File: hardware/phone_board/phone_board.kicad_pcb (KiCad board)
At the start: 4 copper layers, 66 x 36 mm, 70 parts, among them J1 TYPE-C-31-M-12, J2 LiPo 1S, Q1 AO3401A, SW1 POWER, SW2 RESET, SW3 BOOT, U1 USBLC6-2SC6, U2 BQ24073RGTR, U3 AP2112K-3.3, U4 TPS61023DRLR, U5 ESP32-S3-MINI-1-N8, U6 ADS1115IDGSR, U7 SHT40-AD1B

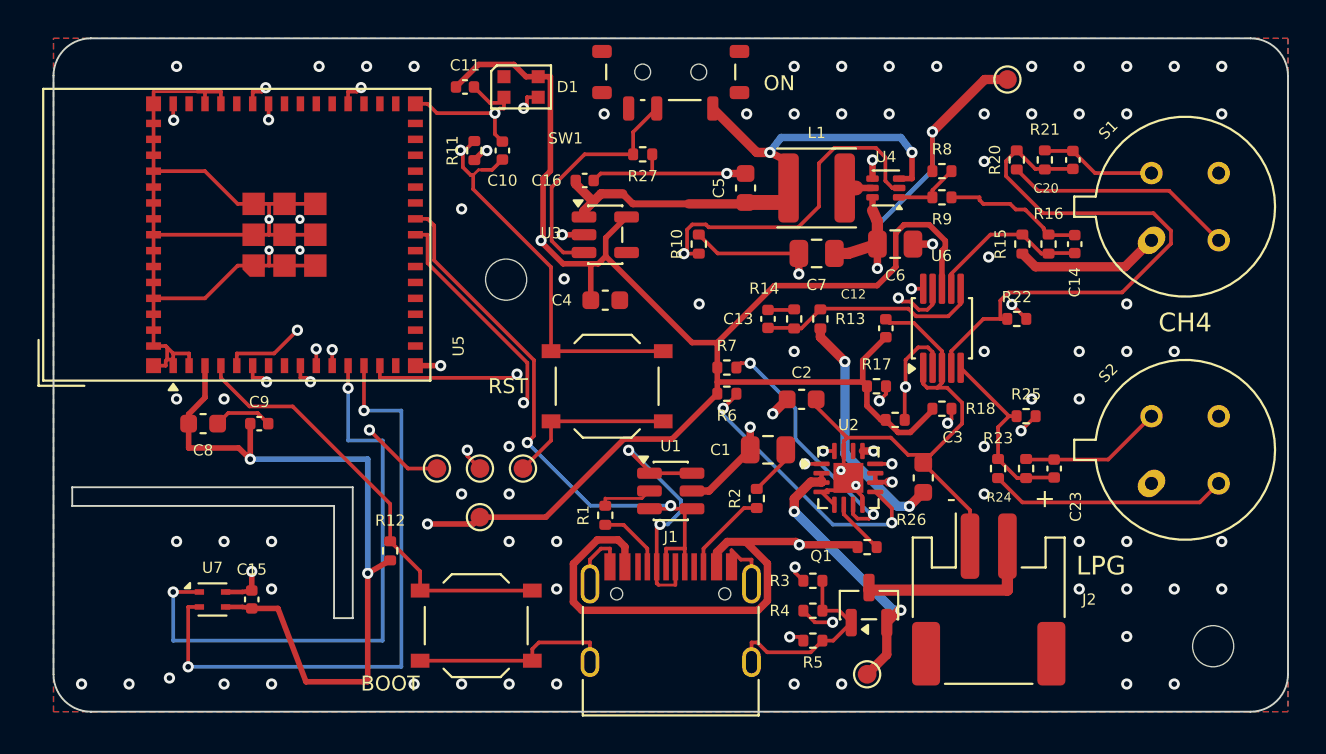
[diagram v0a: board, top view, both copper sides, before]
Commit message: Phone board rev C: compact the layout to 60 x 33 mm
Same schematic, parts and block arrangement as the fabricated rev B, with the
empty board area removed. The hand-routed blocks move as rigid units (MCU
column and SHT40 tongue 2 mm up, power/USB column with the boost loop 2 mm
left); only the free-form right third is re-packed: cans flush at the right
edge, JST-PH under them exiting through the right edge, ADC and sensor
networks in one column, RESET above BOOT, serial test pads as a labelled
2 x 2 grid. Adds a GND via stub for the USB ESD diode, whose pour island had
none. Re-routed with Freerouting: 0 DRC, 0 unconnected, 0 parity, ERC clean.
Regenerated fab files, JLC placement and renders.

Enclosure: parameters updated for rev C and the battery opening moved to the
right wall; STLs not regenerated (no OpenSCAD here) and the H1 hold-down boss
now sits under a 60 x 35 mm cell, noted in its README.
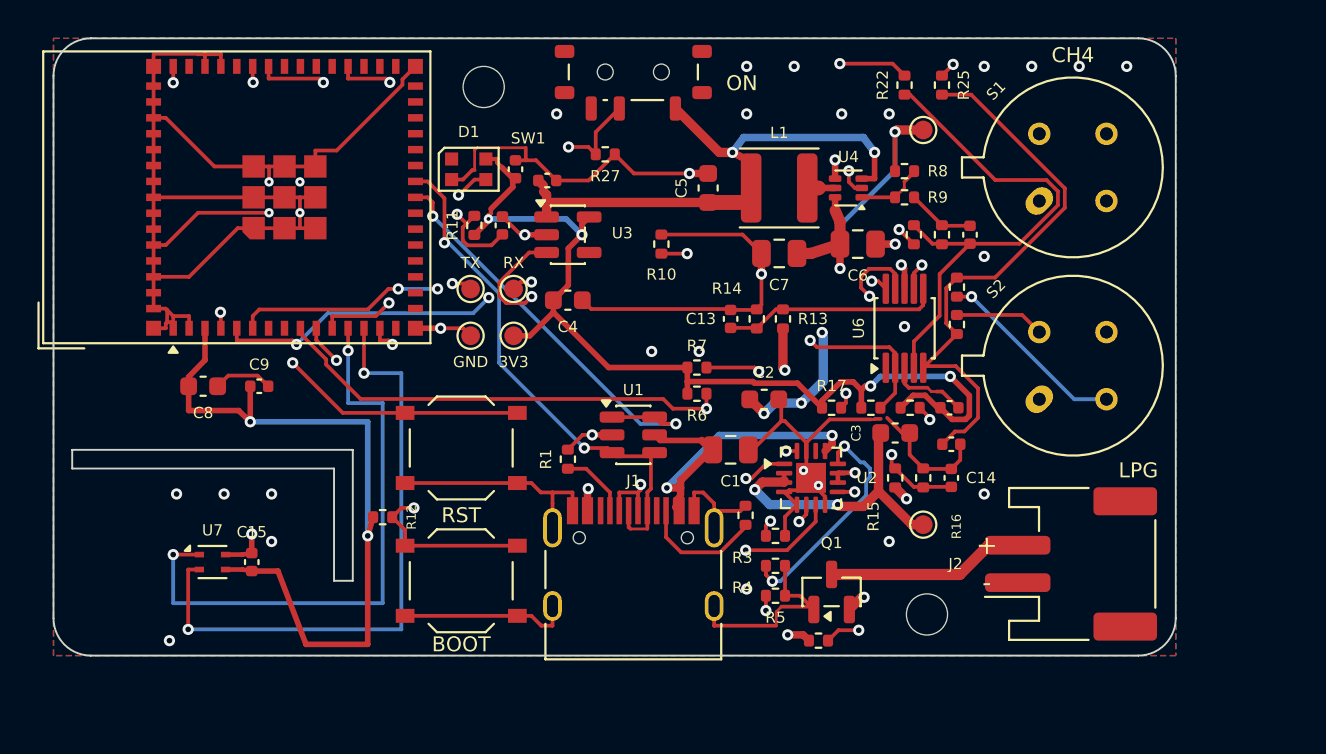
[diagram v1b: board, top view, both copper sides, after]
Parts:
- moved R25 18.3 mm to (47.5, 2.50), turned to 90 degrees
- moved H1 15.4 mm to (46.7, 30.8)
- moved R15 14.2 mm to (45.0, 23.5)
- moved R16 14.2 mm to (46.5, 23.5)
- moved C14 14.1 mm to (48.0, 23.5)
- moved R22 13.9 mm to (45.5, 2.50), turned to 90 degrees
- moved H2 10.4 mm to (23.0, 2.60)
- moved R23 9.95 mm to (48.3, 13.3)
- moved TP4 9.87 mm to (24.6, 15.9)
- moved TP1 9.77 mm to (22.3, 13.4)
- moved TP2 9.77 mm to (24.6, 13.4)
- moved TP5 8.54 mm to (46.5, 26.0)
- moved R24 8.54 mm to (48.3, 15.3)
- moved SW2 8.47 mm to (21.8, 21.9)
- moved TP3 7.63 mm to (22.3, 15.9)
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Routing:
- net /LPG_TAP: track 10.0 -> 30.6 mm
- net /+3V3: track 139.3 -> 119.1 mm, vias 5 -> 7
- net /VBUS: track 51.2 -> 37.5 mm, vias 3 -> 4
- net /LPG_FB: track 55.9 -> 45.6 mm, vias 2 -> 3
- net /VSYS: track 65.8 -> 55.8 mm, vias 4 -> 6
- net /GND: track 188.4 -> 196.8 mm, vias 85 -> 36
- net /HTR_SENSE: track 8.71 -> 16.7 mm, vias 0 -> 2
- net /BAT_CELL: track 9.89 -> 17.5 mm
- net /BQ_EN1: track 2.99 -> 10.1 mm, vias 0 -> 2
- net /ESP_EN: track 40.4 -> 47.2 mm, vias 2 -> 3
- net /PWR_EN: track 12.9 -> 19.3 mm, vias 0 -> 2
- net /+5V_HTR: track 65.0 -> 59.4 mm, vias 2 -> 3
- net /RXD0: track 29.8 -> 24.6 mm
- net /PGOOD_N: track 38.2 -> 43.3 mm
- net /HTR_EN: track 40.1 -> 35.0 mm, vias 2 -> 3
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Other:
- board size 66 x 36 mm -> 60 x 33 mm
- board text added: "3V3"
- board text added: "CH4 detector rev C"
- board text added: "GND"
- board text added: "RX"
- board text added: "TX"
- board text removed: "CH4 detector rev B"

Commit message: Phone board rev C: give the board a business end
Sensors at the front: both Figaro cans overhang the right edge by ~1 mm with a
7 mm notch milled between them, so each can stands in air on three sides.
Power at the rear: USB-C on the bottom edge and the battery JST-PH on the top
edge, both beside the ESP32 module and ~30 mm from the heaters, with the
reverse-cell FET next to the JST. SHT40 tongue kept with a 2.5 mm neck and no
copper pour on any layer over the tongue or neck; only its four tracks cross.
Boost loop and ESP32 decoupling moved as rigid units; charger, ADC, buttons
and test pads re-placed. Locked escapes for the boost EN pad and an In2 SDA
trunk, plus GND stubs for pads the pours fenced off. 60 x 33 mm unchanged.
0 DRC, 0 unconnected, 0 parity, ERC clean; fab files, JLC placement and
renders regenerated. Enclosure parameters and READMEs updated to match.
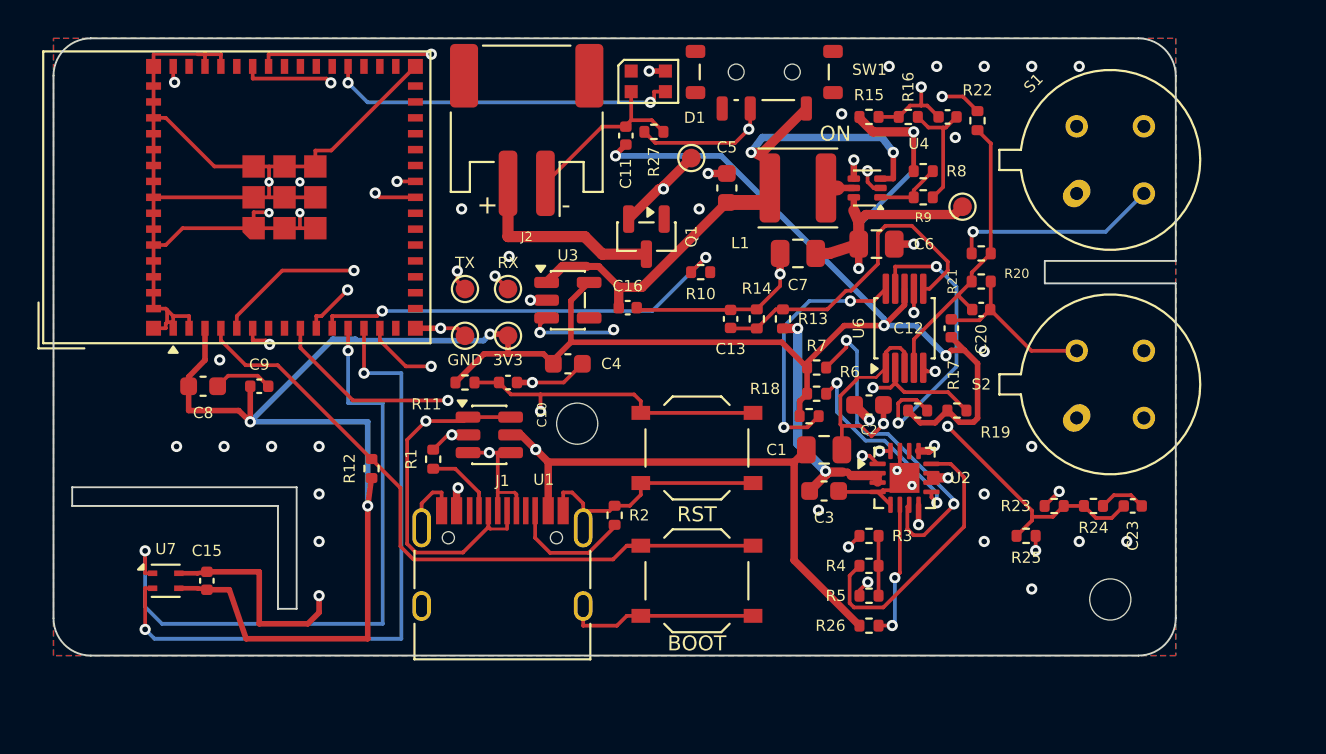
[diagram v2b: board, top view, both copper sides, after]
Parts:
- moved J2 37.2 mm to (25.3, 4.90), turned to 180 degrees
- moved R25 24.5 mm to (52.0, 26.6), turned to 0 degrees
- moved TP5 23.2 mm to (34.1, 6.40)
- moved Q1 21.4 mm to (31.7, 10.6), turned to -90 degrees
- moved R15 19.4 mm to (43.6, 4.20), turned to 0 degrees
- moved R16 19.3 mm to (45.7, 4.20), turned to 0 degrees
- moved C14 19.3 mm to (47.8, 4.20), turned to 0 degrees
- moved H2 18.7 mm to (28.0, 20.6)
- moved R23 12.8 mm to (53.5, 25.0), turned to 0 degrees
- moved SW2 12.6 mm to (34.4, 21.9)
- moved SW3 12.6 mm to (34.4, 29.0)
- moved R24 12.1 mm to (55.6, 25.0), turned to 0 degrees
- moved D1 10.7 mm to (31.8, 2.30)
- moved C23 10.2 mm to (57.7, 25.0)
- moved H1 9.83 mm to (56.5, 30.0)
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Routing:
- net /VBUS: track 37.5 -> 60.2 mm, vias 4 -> 3
- net /GND: track 196.8 -> 180.1 mm, vias 36 -> 42
- net /I2C_SDA: track 71.3 -> 87.7 mm
- net /+3V3: track 119.1 -> 133.0 mm
- net /LPG_TAP: track 30.6 -> 17.7 mm, vias 0 -> 2
- net /CH4_TAP: track 28.1 -> 15.8 mm
- net /BOOT: track 28.3 -> 36.8 mm, vias 2 -> 0
- net /PWR_EN: track 19.3 -> 27.2 mm, vias 2 -> 3
- net /USB_DN: track 30.4 -> 38.2 mm, vias 3 -> 2
- net /BAT_CELL: track 17.5 -> 10.6 mm
- net /LED_DIN: track 12.3 -> 18.7 mm
- net /VBAT_SENSE: track 11.7 -> 17.8 mm
- net /HTR_SENSE: track 16.7 -> 22.6 mm
- net /PGOOD_N: track 43.3 -> 49.0 mm
- net /ESP_EN: track 47.2 -> 52.0 mm, vias 3 -> 2
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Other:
- outline, holes or cut-outs redrawn
